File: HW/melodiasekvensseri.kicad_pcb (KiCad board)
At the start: 2 copper layers, 60.6 x 110 mm, 58 parts, among them IC1 74LS138, J1 Conn_02x05_Odd_Even, J2 Clock_In, J3 Gate_Out, J4 CV_Out, J5 Conn_02x03_Odd_Even, J6 Conn_01x04, U1 TLV2372IP

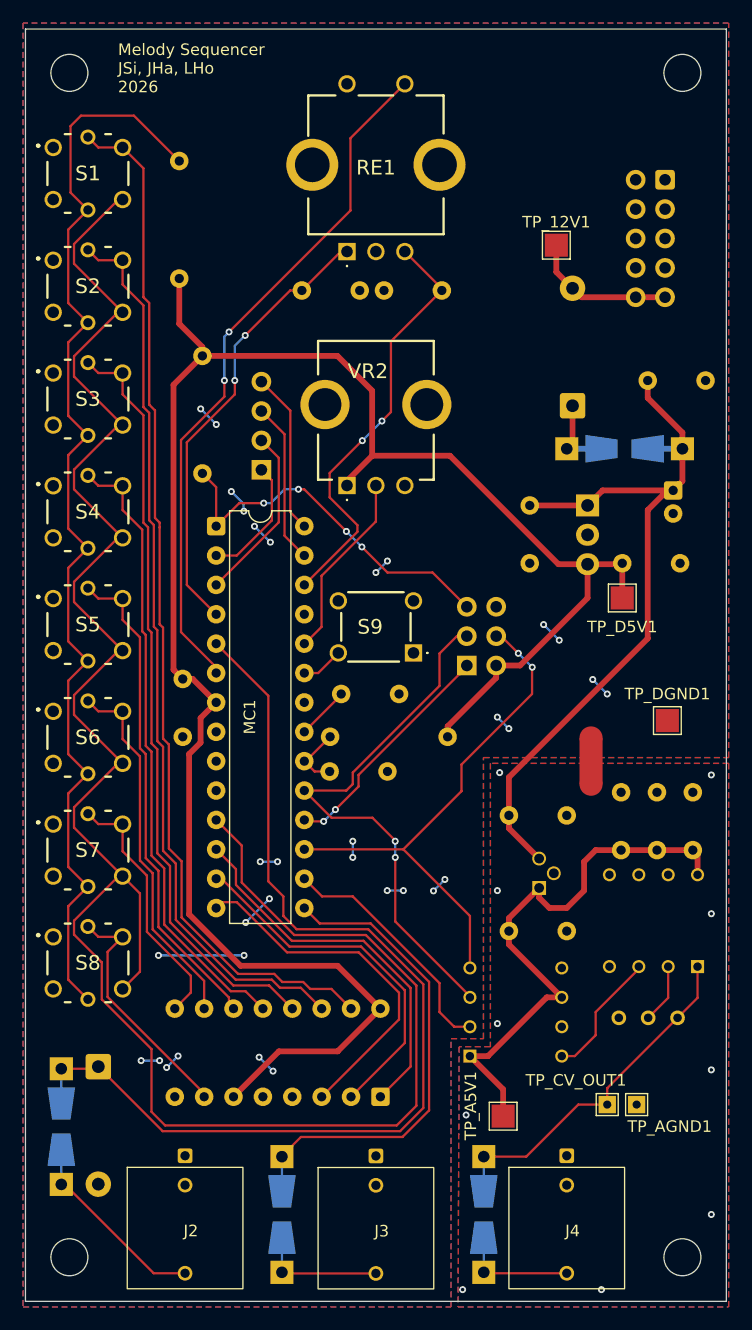
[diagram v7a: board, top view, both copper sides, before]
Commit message: Moved or added decoupling caps, moved test points
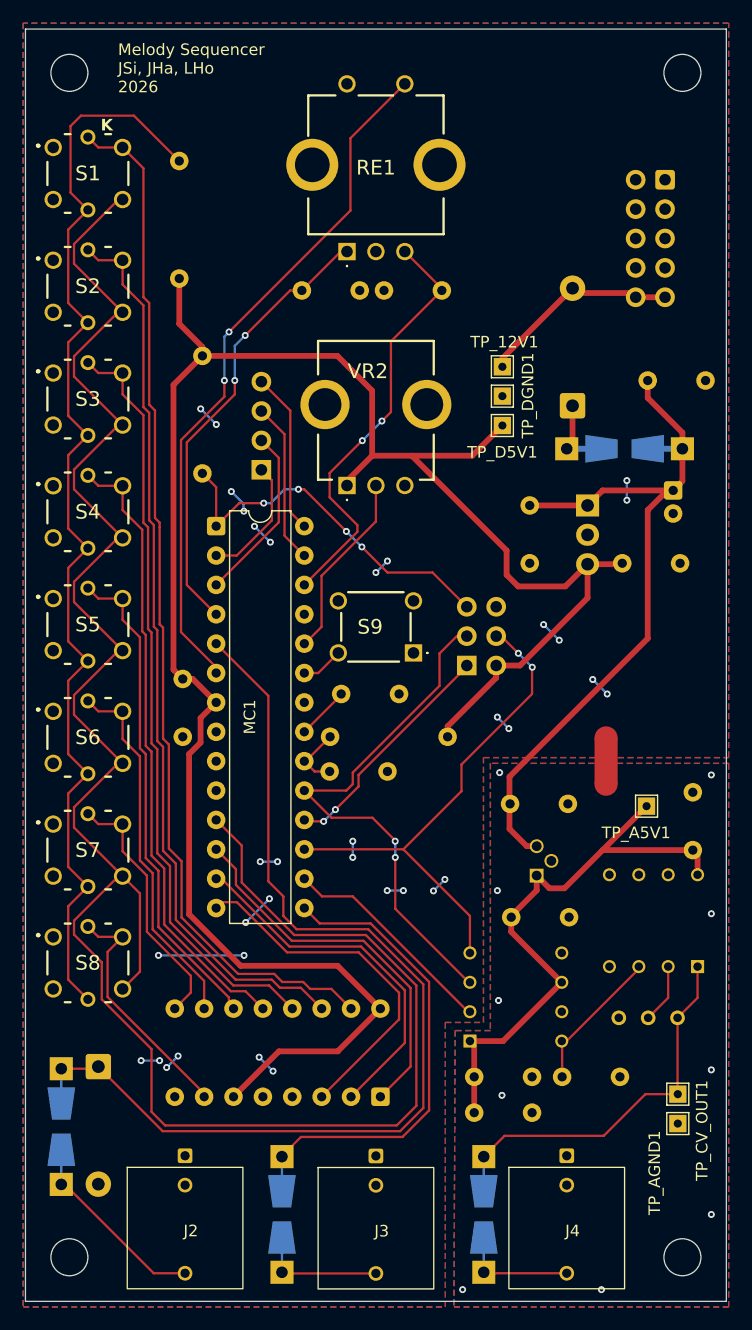
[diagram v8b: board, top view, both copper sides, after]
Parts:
- added C18: 1u, Capacitor_THT:C_Disc_D5.0mm_W2.5mm_P5.00mm, B.Cu at (171.1, 127.1)
- TP_12V1, TP_A5V1, TP_D5V1, TP_DGND1: footprint TestPoint:TestPoint_Pad_2.0x2.0mm -> TestPoint:TestPoint_THTPad_1.5x1.5mm_Drill0.7mm
- moved TP_DGND1 31.5 mm to (160.9, 68.2)
- moved C8 30.5 mm to (158.5, 130.2), turned to 0 degrees
- moved TP_A5V1 29.5 mm to (173.4, 103.7), turned to -90 degrees
- moved C9 26.9 mm to (163.5, 127.1), turned to 180 degrees
- moved TP_D5V1 18.2 mm to (160.9, 70.8)
- moved TP_12V1 11.5 mm to (160.9, 65.7), turned to 180 degrees
- moved TP_CV_OUT1 6.17 mm to (176.1, 128.6), turned to 0 degrees
- moved TP_AGND1 3.92 mm to (176.1, 131.1), turned to 180 degrees
- moved NT1 1.30 mm to (169.9, 99.8)
- moved DAC1 1.30 mm to (162.1, 120.2)
- moved C16 1.22 mm to (166.7, 113.3)
- moved REG2 1.09 mm to (163.9, 109.7)
- moved C17 1.00 mm to (166.6, 103.5)
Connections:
- C8 pad 1: A_GND -> A_+5V
- C8 pad 2: A_+5V -> A_GND
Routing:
- net D_+5V: track 169.8 -> 178.5 mm
- net Net-(D1-A): track 12.6 -> 16.5 mm
- net CV_Out: track 30.7 -> 33.7 mm
- net DAC_CS: track 21.1 -> 18.9 mm
- net A_+5V: track 49.2 -> 51.2 mm
- net D_GND: track 33.5 -> 35.2 mm, vias 32 -> 34
- net SPI_MOSI: track 45.4 -> 44.1 mm
- net SPI_SCK: track 47.6 -> 46.3 mm
- net Net-(DAC1-VOUT): track 11.0 -> 11.9 mm
- net +12V: track 65.6 -> 64.9 mm
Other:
- board text added: "+"
- board text added: "1"
- board text added: "K"
